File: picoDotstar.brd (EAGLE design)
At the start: 65 x 65 mm, 17 parts

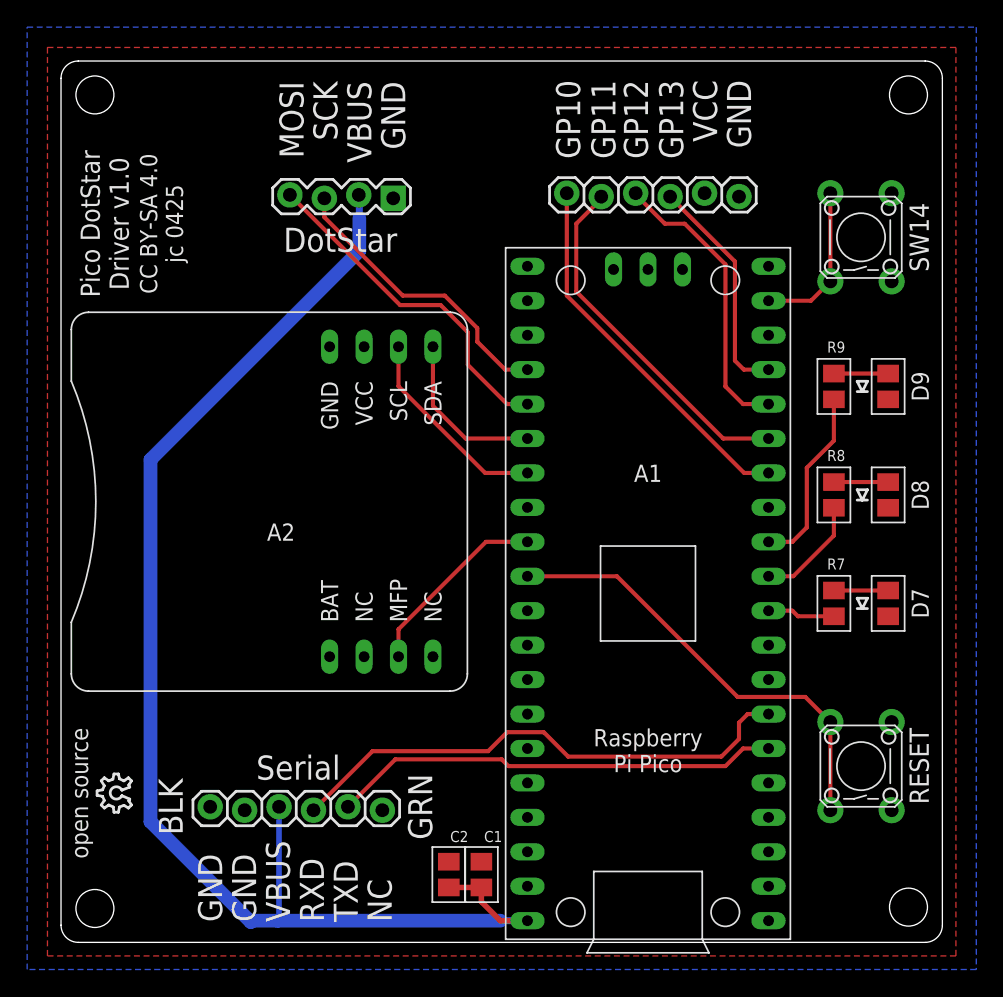
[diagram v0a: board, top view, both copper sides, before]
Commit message: Move RTC from I2C0 to I2C1.
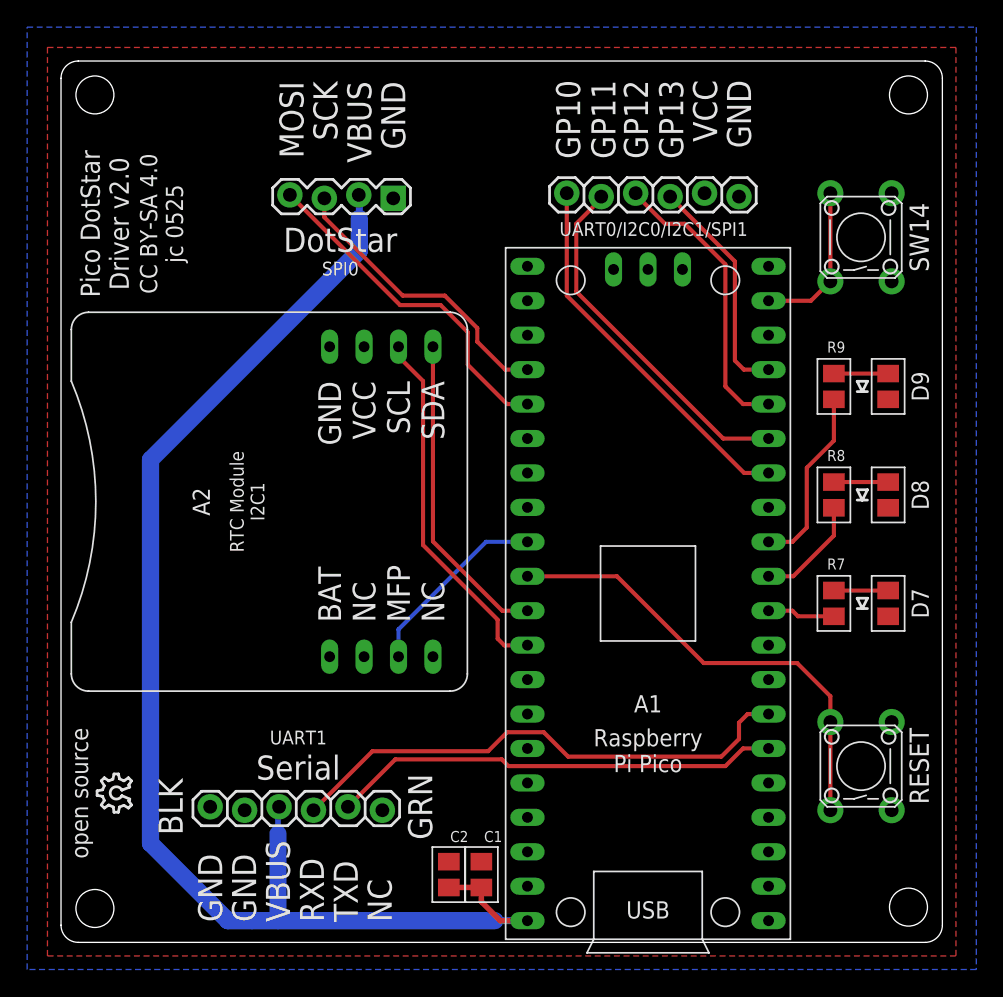
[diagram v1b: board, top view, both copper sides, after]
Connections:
- net SCL: now also A1.P$32; no longer A1.P$27
- net SDA: now also A1.P$31; no longer A1.P$26
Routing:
- net SCL: track 15.1 -> 27.0 mm
- net SDA: track 12.3 -> 23.4 mm
- net RUN: track 33.3 -> 34.4 mm
- net VBUS: track 99.4 -> 100.3 mm
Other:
- board text added: "CC BY-SA 4.0 jc 0525"
- board text added: "Pico DotStar Driver v2.0"
- board text added: "RTC Module I2C1"
- board text added: "SPI0"
- board text added: "UART0/I2C0/I2C1/SPI1"
- board text added: "UART1"
- board text removed: "CC BY-SA 4.0 jc 0425"
- board text removed: "Pico DotStar Driver v1.0"
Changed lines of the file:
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@@
 <text x="64" y="52" size="1.4224" layer="21" ratio="16" rot="R90" align="bottom-center">SW14</text>
 <text x="5" y="53" size="1.4224" layer="21" ratio="16" rot="R90" align="bottom-center">Pico DotStar
-Driver v1.0</text>
+Driver v2.0</text>
 <text x="9" y="53" size="1.27" layer="21" ratio="16" rot="R90" align="bottom-center">CC BY-SA 4.0
-jc 0425</text>
+jc 0525</text>
 <text x="2" y="11" size="1.27" layer="21" ratio="16" rot="R90" align="bottom-center">open source</text>
-<text x="3" y="52" size="1.778" layer="22" ratio="16" rot="SMR270">Pico DotStar Driver v1.0</text>
-<text x="6" y="52" size="1.4224" layer="22" ratio="16" rot="SMR270">CC BY-SA 4.0 jc 0425</text>
+<text x="3" y="52" size="1.778" layer="22" ratio="16" rot="SMR270">Pico DotStar Driver v2.0</text>
+<text x="6" y="52" size="1.4224" layer="22" ratio="16" rot="SMR270">CC BY-SA 4.0 jc 0525</text>
 <text x="12" y="52" size="1.4224" layer="22" ratio="16" rot="SMR270">open source</text>
 <text x="9" y="52" size="1.4224" layer="22" ratio="16" rot="SMR270">bit.ly/pico-ds</text>
+<text x="15" y="32.5" size="1.016" layer="21" ratio="16" rot="R90" align="bottom-center">RTC Module
+I2C1</text>
+<text x="20.6" y="50.2" size="1.016" layer="21" ratio="16" rot="R180" align="bottom-center">SPI0</text>
+<text x="17.5" y="14.6" size="1.016" layer="21" ratio="16" align="bottom-center">UART1</text>
+<text x="43.7" y="52.1" size="1.016" layer="21" ratio="16" align="bottom-center">UART0/I2C0/I2C1/SPI1</text>
 </plain>
 <attributes>
@@
 <elements>
 <element name="A1" library="_jc" package="PICO" value="RPI PICO" x="53.79" y="51.23" smashed="yes" rot="R180">
-<attribute name="NAME" x="43.29" y="35.23" size="1.27" layer="25" ratio="14" rot="R180" align="bottom-center"/>
+<attribute name="NAME" x="43.29" y="18.23" size="1.27" layer="25" ratio="14" rot="R180" align="bottom-center"/>
 <attribute name="VALUE" x="43.29" y="37.73" size="1.27" layer="27" ratio="14" rot="R180" align="bottom-center"/>
 </element>
 <element name="A2" library="_jc" package="RTC79412" value="RTC" x="16" y="32.5" smashed="yes" rot="R90">
-<attribute name="NAME" x="15.19" y="29.62" size="1.27" layer="25"/>
-<attribute name="VALUE" x="10.92" y="28.69" size="1.27" layer="27" rot="R90"/>
+<attribute name="NAME" x="10.98" y="32.5" size="1.27" layer="25" ratio="16" rot="R90" align="bottom-center"/>
+<attribute name="VALUE" x="10.92" y="32.5" size="1.27" layer="27" ratio="16" rot="R90" align="bottom-center"/>
 </element>
 <element name="S1" library="_jc" package="B3F-10XXOCT" value="RESET" x="59" y="13" smashed="yes" rot="R90">
@@
 <signals>
 <signal name="GND">
-<polygon width="0.1524" layer="1">
+<polygon width="0.1524" layer="1" isolate="0.254">
 <vertex x="-1" y="66"/>
 <vertex x="66" y="66"/>
@@
 </signal>
 <signal name="VCC">
-<polygon width="0.1524" layer="16">
+<polygon width="0.1524" layer="16" isolate="0.254">
 <vertex x="-2.5" y="67.5"/>
 <vertex x="67.5" y="67.5"/>
@@
 <contactref element="A1" pad="P$30"/>
 <wire x1="34.4" y1="27" x2="41" y2="27" width="0.3048" layer="1"/>
-<wire x1="54.8906" y1="18.1" x2="56.7394" y2="16.2512" width="0.3048" layer="1"/>
-<wire x1="41" y1="27" x2="49.9" y2="18.1" width="0.3048" layer="1"/>
-<wire x1="49.9" y1="18.1" x2="54.8906" y2="18.1" width="0.3048" layer="1"/>
+<wire x1="56.7394" y1="18.1512" x2="54.2906" y2="20.6" width="0.3048" layer="1"/>
+<wire x1="56.7394" y1="18.1512" x2="56.7394" y2="16.2512" width="0.3048" layer="1"/>
+<wire x1="41" y1="27" x2="47.4" y2="20.6" width="0.3048" layer="1"/>
+<wire x1="47.4" y1="20.6" x2="54.2906" y2="20.6" width="0.3048" layer="1"/>
 <wire x1="56.7394" y1="16.2512" x2="56.7394" y2="9.7488" width="0.3048" layer="1"/>
 </signal>
@@
 <contactref element="JP2" pad="3"/>
 <contactref element="JP1" pad="2"/>
-<wire x1="6.6" y1="8.9" x2="14" y2="1.5" width="1.016" layer="16"/>
-<wire x1="6.6" y1="35.6" x2="22" y2="51" width="1.016" layer="16"/>
-<wire x1="6.6" y1="8.9" x2="6.6" y2="35.6" width="1.016" layer="16"/>
-<wire x1="14" y1="1.5" x2="14.1" y2="1.6" width="1.016" layer="16"/>
-<wire x1="14.1" y1="1.6" x2="16" y2="1.6" width="1.016" layer="16"/>
-<wire x1="16" y1="1.6" x2="32.4" y2="1.6" width="1.016" layer="16"/>
-<wire x1="16.08" y1="10" x2="16.08" y2="1.68" width="0.4064" layer="16"/>
+<wire x1="22" y1="51" x2="6.6" y2="35.6" width="1.27" layer="16"/>
+<wire x1="14.1" y1="1.6" x2="16" y2="1.6" width="1.27" layer="16"/>
+<wire x1="16" y1="1.6" x2="32" y2="1.6" width="1.27" layer="16"/>
 <wire x1="16.08" y1="1.68" x2="16" y2="1.6" width="0.4064" layer="16"/>
-<wire x1="22" y1="53.4" x2="22" y2="51" width="1.016" layer="16"/>
-<wire x1="32.4" y1="1.6" x2="34.4" y2="1.6" width="0.508" layer="16"/>
+<wire x1="22" y1="53.4" x2="22" y2="51" width="1.27" layer="16"/>
+<wire x1="32" y1="1.6" x2="34.4" y2="1.6" width="0.508" layer="16"/>
 <wire x1="21.96" y1="55.127" x2="22" y2="55.087" width="0.508" layer="16"/>
 <wire x1="22" y1="55.087" x2="22" y2="53.4" width="0.508" layer="16"/>
@@
 <wire x1="32.4" y1="1.6" x2="31" y2="3" width="0.4064" layer="1"/>
 <wire x1="31" y1="3" x2="31" y2="4.05" width="0.4064" layer="1"/>
+<wire x1="16.08" y1="10" x2="16" y2="9.92" width="0.4064" layer="16"/>
+<wire x1="16" y1="9.92" x2="16" y2="8" width="0.4064" layer="16"/>
+<wire x1="16" y1="8" x2="16" y2="1.76" width="1.27" layer="16"/>
+<wire x1="16" y1="1.76" x2="16.08" y2="1.68" width="1.27" layer="16"/>
+<wire x1="6.6" y1="7.3" x2="12.3" y2="1.6" width="1.27" layer="16"/>
+<wire x1="12.3" y1="1.6" x2="14.1" y2="1.6" width="1.27" layer="16"/>
+<wire x1="6.6" y1="35.6" x2="6.6" y2="7.3" width="1.27" layer="16"/>
 </signal>
 <signal name="RXD">
@@
 <signal name="SCL">
 <contactref element="A2" pad="6"/>
-<contactref element="A1" pad="P$27"/>
-<wire x1="34.4" y1="34.62" x2="31.28" y2="34.62" width="0.3048" layer="1"/>
-<wire x1="24.89" y1="41.01" x2="24.89" y2="43.93" width="0.3048" layer="1"/>
-<wire x1="31.28" y1="34.62" x2="24.89" y2="41.01" width="0.3048" layer="1"/>
+<contactref element="A1" pad="P$32"/>
+<wire x1="24.89" y1="43.93" x2="24.89" y2="43.21" width="0.3048" layer="1"/>
+<wire x1="26.7" y1="29.3" x2="32.2" y2="23.8" width="0.3048" layer="1"/>
+<wire x1="32.2" y1="22.4" x2="32.7" y2="21.9" width="0.3048" layer="1"/>
+<wire x1="32.7" y1="21.9" x2="34.38" y2="21.9" width="0.3048" layer="1"/>
+<wire x1="34.38" y1="21.9" x2="34.4" y2="21.92" width="0.3048" layer="1"/>
+<wire x1="24.89" y1="43.21" x2="26.7" y2="41.4" width="0.3048" layer="1"/>
+<wire x1="26.7" y1="41.4" x2="26.7" y2="29.3" width="0.3048" layer="1"/>
+<wire x1="32.2" y1="23.8" x2="32.2" y2="22.4" width="0.3048" layer="1"/>
 </signal>
 <signal name="SDA">
 <contactref element="A2" pad="5"/>
-<contactref element="A1" pad="P$26"/>
-<wire x1="34.4" y1="37.16" x2="29.84" y2="37.16" width="0.3048" layer="1"/>
-<wire x1="27.43" y1="39.57" x2="27.43" y2="43.93" width="0.3048" layer="1"/>
-<wire x1="29.84" y1="37.16" x2="27.43" y2="39.57" width="0.3048" layer="1"/>
+<contactref element="A1" pad="P$31"/>
+<wire x1="27.43" y1="43.93" x2="27.43" y2="29.57" width="0.3048" layer="1"/>
+<wire x1="32.54" y1="24.46" x2="34.4" y2="24.46" width="0.3048" layer="1"/>
+<wire x1="27.43" y1="29.57" x2="32.54" y2="24.46" width="0.3048" layer="1"/>
 </signal>
 <signal name="N$3">
@@
 <contactref element="A2" pad="3"/>
 <contactref element="A1" pad="P$29"/>
-<wire x1="34.4" y1="29.54" x2="31.34" y2="29.54" width="0.3048" layer="1"/>
-<wire x1="24.89" y1="23.09" x2="24.89" y2="21.07" width="0.3048" layer="1"/>
-<wire x1="31.34" y1="29.54" x2="24.89" y2="23.09" width="0.3048" layer="1"/>
+<wire x1="34.4" y1="29.54" x2="31.34" y2="29.54" width="0.3048" layer="16"/>
+<wire x1="24.89" y1="23.09" x2="24.89" y2="21.07" width="0.3048" layer="16"/>
+<wire x1="31.34" y1="29.54" x2="24.89" y2="23.09" width="0.3048" layer="16"/>
 </signal>
 <signal name="GP10">
